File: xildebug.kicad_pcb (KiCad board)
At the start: 2 copper layers, 42 x 46.2 mm, 66 parts, among them J1 USB_B_Micro, J2 Conn_STM_SWD, J3 Conn_Ext1, J4 Conn_Ext2, J5 Conn_DUT, J6 Conn_DUT_VDD, SW1 BOOT0, U1 XC6206P332MR, U2 MAX14662, U3 STM32L433CCUx, U4 TS5A3167, U5 MIC5219YMT, U6 TS5A3167, U7 MCP4018, U8 TS5A3167

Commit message: Minification
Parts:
- removed C11, C15: 1uF, Capacitor_SMD:C_0603_1608Metric
- removed C12, C14, C17, C18, C19, C8: 0.1uF, Capacitor_SMD:C_0603_1608Metric
- removed C13: 4.7uF, Capacitor_SMD:C_0603_1608Metric
- removed C16: 470pF, Capacitor_SMD:C_0603_1608Metric
- removed D4: LED_RGB, LED_SMD_Extra:LED_RGB_0606_1616Metric
- removed the G*** at (228.9, 85.4)
- removed the G*** at (226.4, 62.4)
- removed J4: Conn_Ext2, Connector_PinHeader_2.54mm:PinHeader_1x12_P2.54mm_Vertical
- removed J6: Conn_DUT_VDD, Connector_PinHeader_2.54mm:PinHeader_1x03_P2.54mm_Horizontal
- removed L1: FB, Inductor_SMD:L_0603_1608Metric
- removed R11, R15, R17: 10K, Resistor_SMD:R_0603_1608Metric
- removed R12, R14: TBD, Resistor_SMD:R_0603_1608Metric
- removed R13: 510R, Resistor_SMD:R_0603_1608Metric
- removed R16: 33R, Resistor_SMD:R_0603_1608Metric
- removed R18: 1.8R, Resistor_SMD:R_0603_1608Metric
- removed R19, R20, R21, R22: 100K, Resistor_SMD:R_0603_1608Metric
- removed R4, R5, R6: 360R, Resistor_SMD:R_0603_1608Metric
- removed U4, U6, U8: TS5A3167, Package_TO_SOT_SMD:SOT-23-5
- removed U5: MIC5219YMT, Package_TO_SOT_SMD:SOT-23-5
- removed U7: MCP4018, Package_TO_SOT_SMD:SOT-363_SC-70-6
- added G***: LOGO, Symbol_Extra:xil_5000, B.Cu at (220.0, 86.7)
- added G***: LOGO, Symbol_Extra:oshw_crop_10000, F.Cu at (227.8, 93.0)
- added Q1: FDN340P, Package_TO_SOT_SMD:SOT-23, F.Cu at (211.1, 66.2)
- J2: footprint Connector_PinHeader_2.54mm:PinHeader_1x04_P2.54mm_Vertical -> Connector_JST:JST_SH_BM04B-SRSS-TB_1x04-1MP_P1.00mm_Vertical
- J3: value Conn_Ext1 -> Conn_GPIO; footprint Connector_PinHeader_2.54mm:PinHeader_1x11_P2.54mm_Vertical -> Connector_PinHeader_2.54mm:PinHeader_1x04_P2.54mm_Vertical
- moved J3 33.7 mm to (229.4, 74.2)
- moved D6 18.7 mm to (219.7, 68.2), turned to 270 degrees
- moved C9 18.5 mm to (211.1, 89.0)
- moved U1 18.5 mm to (211.1, 86.5), turned to 180 degrees
- moved D5 16.9 mm to (221.6, 68.2), turned to 90 degrees
- moved D1 16.6 mm to (210.2, 76.8)
- moved D2 16.6 mm to (210.2, 70.3)
- moved D3 16.6 mm to (210.2, 73.6)
- moved R1 13.3 mm to (211.8, 76.8)
- moved R2 13.3 mm to (211.8, 70.3)
- moved R3 13.3 mm to (211.8, 73.5)
- moved U2 11.2 mm to (220.0, 73.6)
- moved J2 10.4 mm to (228.6, 87.5), turned to 270 degrees
- moved R23 9.76 mm to (222.2, 78.8), turned to 90 degrees
- moved C3 7.58 mm to (217.9, 68.2), turned to 90 degrees
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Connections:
- net /POT_SCL renamed /STM_SCL
- net /POT_SDA renamed /STM_SDA
- C7 pad 1: Net-(C11-Pad1) -> +3V3
- D5 pad 1: /DUT_UART_TX_B -> Net-(D5-Pad1)
- D5 pad 2: Net-(D5-Pad2) -> /DUT_UART_RX_B
- D6 pad 1: Net-(D6-Pad1) -> /DUT_UART_TX_B
- D6 pad 2: /DUT_UART_RX_B -> Net-(D6-Pad2)
- J3 pad 1: +5V -> /GPIO0_B
- J3 pad 2: +3V3 -> /GPIO1_B
- J3 pad 3: GND -> /GPIO2_B
- J3 pad 4: /PB15 -> /GPIO3_B
- J5 pad 1: /DUT_VDD_OUT -> Net-(J5-Pad1)
- U2 pad 18: /DUT_SWCLK_B -> Net-(D5-Pad1)
- U2 pad 2: /DUT_UART_RX_A -> /DUT_SWCLK_A
- U2 pad 20: Net-(D5-Pad2) -> Net-(D6-Pad2)
- U2 pad 21: Net-(D6-Pad1) -> /DUT_SWCLK_B
- U2 pad 5: /DUT_SWCLK_A -> /DUT_UART_RX_A
- U3 pad 10: /DUT_VDD_IN_DIV -> Net-(U3-Pad10)
- U3 pad 11: /DUT_VDD_OUT_DIV -> Net-(U3-Pad11)
- U3 pad 12: /PA2 -> /DUT_UART_TX_A
- U3 pad 13: /PA3 -> /DUT_UART_RX_A
- U3 pad 14: /DUT_SWD_LED -> /DUT_SWDIO_A
- U3 pad 15: /SHUNT1_EN -> /DUT_SWCLK_A
- U3 pad 16: /SHUNT2_EN -> /DUT_VDD_CTRL
- U3 pad 17: /PA7 -> /DUT_UART_TX_LED
- U3 pad 18: /DUT_VDD_EN -> /DUT_UART_RX_LED
- U3 pad 19: /DUT_SWCLK_A -> /DUT_SWD_LED
- U3 pad 2: /GPIO2_A -> Net-(U3-Pad2)
- U3 pad 20: /DUT_SWDIO_A -> Net-(U3-Pad20)
- U3 pad 21: /DUT_UART_TX_A -> Net-(U3-Pad21)
- U3 pad 22: /DUT_UART_RX_A -> Net-(U3-Pad22)
- U3 pad 25: /LED_RGB_B -> Net-(U3-Pad25)
- U3 pad 26: /PB13 -> Net-(U3-Pad26)
- U3 pad 27: /PB14 -> Net-(U3-Pad27)
- U3 pad 28: /PB15 -> Net-(U3-Pad28)
- U3 pad 29: /LED_RGB_G -> Net-(U3-Pad29)
- U3 pad 3: /GPIO3_A -> /GPIO0_A
- U3 pad 38: /LED_RGB_R -> Net-(U3-Pad38)
- U3 pad 39: /PB3 -> Net-(U3-Pad39)
- U3 pad 4: /PC15 -> /GPIO1_A
- U3 pad 40: /PB4 -> Net-(U3-Pad40)
- U3 pad 41: /PB5 -> Net-(U3-Pad41)
- U3 pad 42: /PB6 -> Net-(U3-Pad42)
- U3 pad 43: /PB7 -> Net-(U3-Pad43)
- U3 pad 45: /GPIO0_A -> Net-(U3-Pad45)
- U3 pad 46: /GPIO1_A -> Net-(U3-Pad46)
- U3 pad 5: /DUT_UART_TX_LED -> /GPIO2_A
- U3 pad 6: /DUT_UART_RX_LED -> /GPIO3_A
- U3 pad 9: Net-(C11-Pad1) -> +3V3
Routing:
- net +5V: track 88.7 -> 15.8 mm, vias 7 -> 2
- net +3V3: track 176.9 -> 112.3 mm, vias 15 -> 17
- net /DUT_VDD_OUT: track 48.1 -> 0.00 mm, vias 1 -> 0
- net /DUT_VDD_IN: track 43.6 -> 0.00 mm, vias 2 -> 0
- net /SHUNT1_EN: track 40.4 -> 0.00 mm, vias 3 -> 0
- net /LED_RGB_R: track 39.0 -> 0.00 mm, vias 4 -> 0
- net /DUT_VDD_EN: track 37.5 -> 0.00 mm, vias 2 -> 0
- net /PC15: track 36.4 -> 0.00 mm, vias 1 -> 0
- net /SHUNT2_EN: track 34.5 -> 0.00 mm, vias 2 -> 0
- net /PB13: track 29.5 -> 0.00 mm
- net /PB14: track 28.0 -> 0.00 mm
- net /PB15: track 26.5 -> 0.00 mm
- net /LED_RGB_G: track 24.9 -> 0.00 mm, vias 2 -> 0
- net /PA2: track 22.9 -> 0.00 mm, vias 1 -> 0
- net /LED_RGB_B: track 22.2 -> 0.00 mm, vias 2 -> 0
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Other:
- board size 42 x 46.2 mm -> 22.4 x 39.7 mm
- board text added: "0"
- board text added: "1"
- board text added: "2"
- board text added: "3"
- board text added: "@arturo182"
- board text added: "BOOT0"
- board text added: "GPIO"
- board text added: "VDD"
- board text added: "xildebug mini rev1"
- board text removed: "3.3V"
- board text removed: "3V"
- board text removed: "5V"
- board text removed: "A2"
- board text removed: "A3"
- board text removed: "A7"
- board text removed: "B13"
- board text removed: "B14"
- board text removed: "B15"
- board text removed: "B3"
- board text removed: "B4"
- board text removed: "B5"
- board text removed: "B6"
- board text removed: "B7"
- board text removed: "C15"
- board text removed: "GPIO0/B8"
- board text removed: "GPIO1/B9"
- board text removed: "GPIO2/C13"
- board text removed: "GPIO3/C14"
- board text removed: "Vdut"
- board text removed: "Vin"
- board text removed: "Vreg"
- board text removed: "xildebug rev1 Apr 2018"

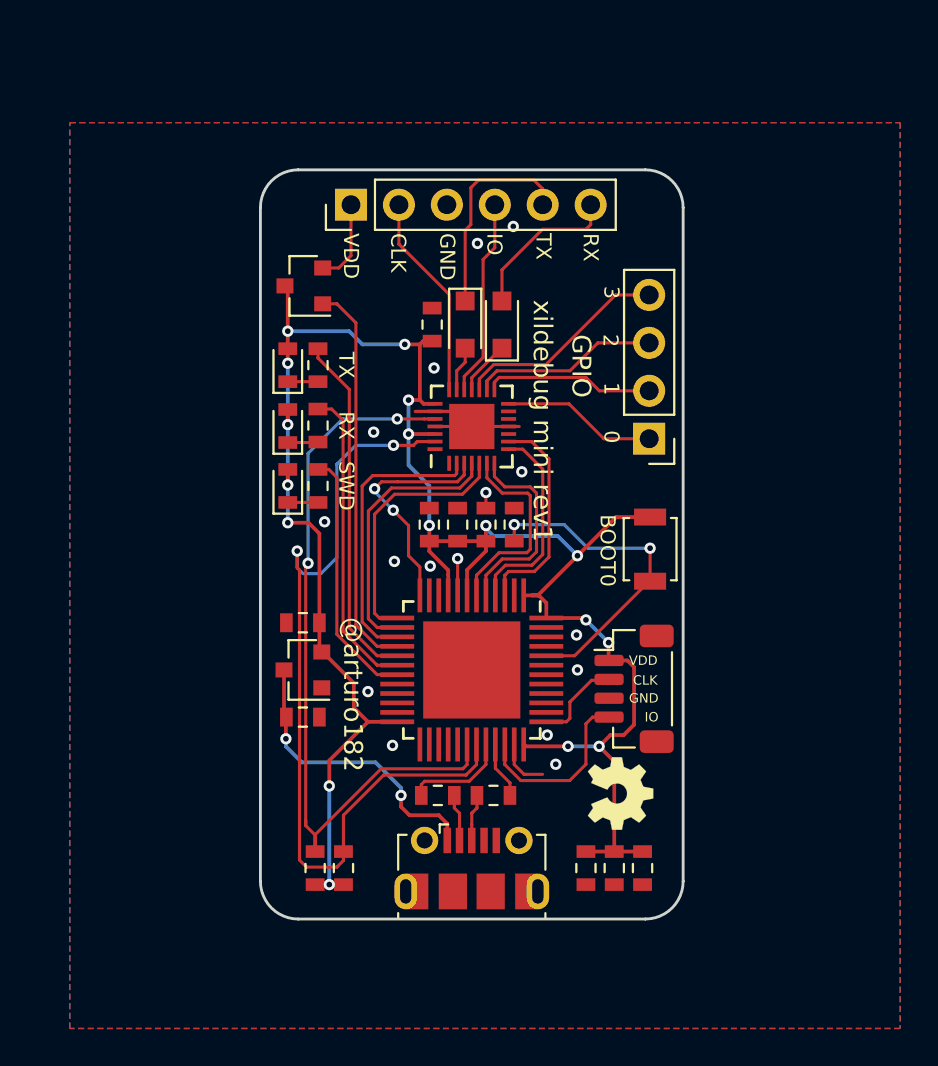
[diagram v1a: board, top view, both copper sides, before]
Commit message: rev2
- Replaced the VDD mosfet with a analog switch
- Changed footprint of STM32L433 to standard one
- Moved UART to USART3, same as xildebug big
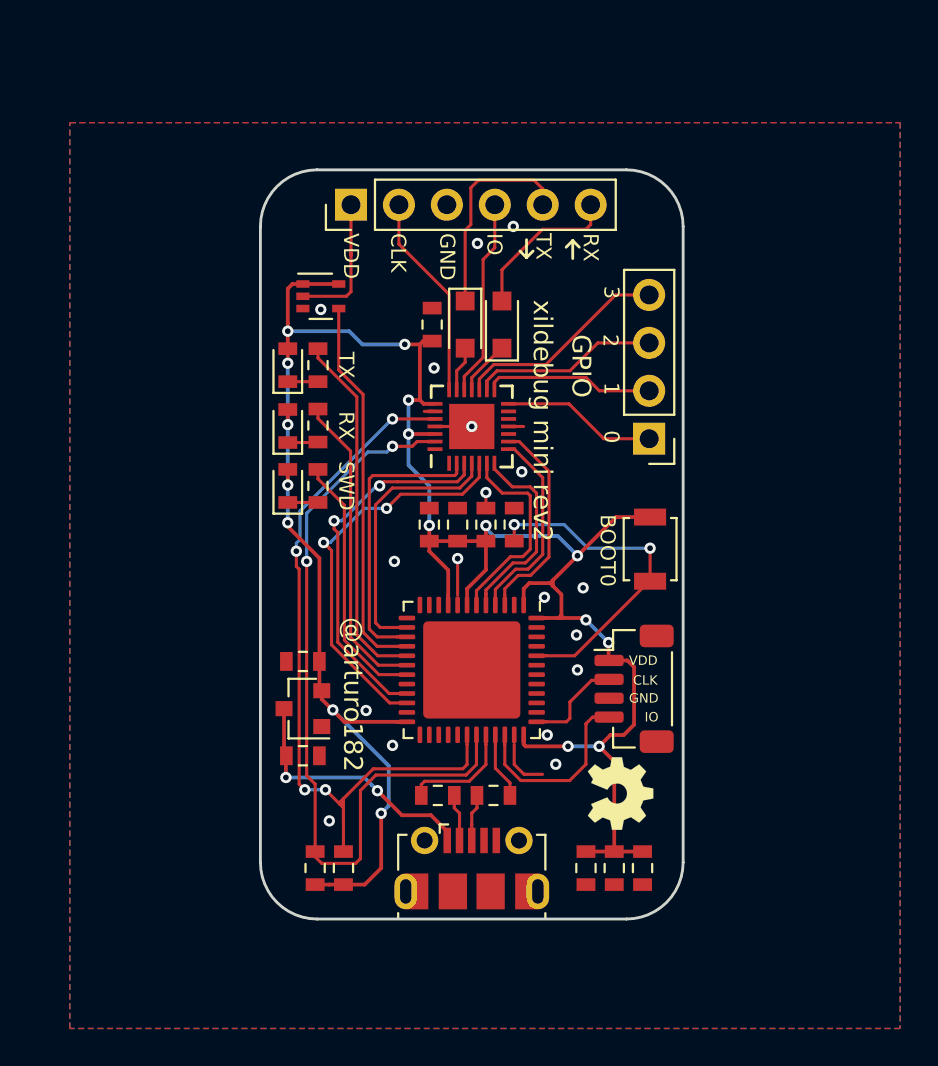
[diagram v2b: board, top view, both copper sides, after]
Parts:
- removed Q1: FDN340P, Package_TO_SOT_SMD:SOT-23
- added U4: SN74LVC1G66, Package_TO_SOT_SMD_Extra:SC-70-5, F.Cu at (212.0, 66.7)
- U3: footprint Package_DFN_QFN_Extra:UFQFPN-48-1EP_7x7mm_P0.5mm_EP5.15x5.15mm -> Package_DFN_QFN:QFN-48-1EP_7x7mm_P0.5mm_EP5.15x5.15mm
- moved C1 2.05 mm to (211.1, 86.0)
- moved C9 2.05 mm to (211.1, 91.0)
- moved U1 2.05 mm to (211.1, 88.5)
- moved R10 1.50 mm to (213.2, 97.0)
- moved R9 1.50 mm to (211.7, 97.0)
- turned G*** to 90 degrees
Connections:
- U3 pad 12: /DUT_UART_TX_A -> Net-(U3-Pad12)
- U3 pad 13: /DUT_UART_RX_A -> Net-(U3-Pad13)
- U3 pad 21: Net-(U3-Pad21) -> /DUT_UART_TX_A
- U3 pad 22: Net-(U3-Pad22) -> /DUT_UART_RX_A
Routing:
- net +3V3: track 112.3 -> 121.8 mm
- net /DUT_UART_RX_A: track 13.7 -> 21.3 mm, vias 0 -> 2
- net /DUT_UART_TX_A: track 12.3 -> 19.8 mm
- net /STM_SDA: track 44.8 -> 41.3 mm
- net GND: track 13.4 -> 10.0 mm, vias 16 -> 18
- net Net-(J5-Pad1): track 4.47 -> 7.41 mm
- net +5V: track 15.8 -> 13.9 mm
- net /STM_SCL: track 40.6 -> 39.7 mm, vias 2 -> 4
- net /DUT_VDD_CTRL: track 20.8 -> 20.3 mm
- net Net-(R8-Pad2): track 5.50 -> 6.02 mm
- net Net-(R7-Pad2): track 3.02 -> 3.53 mm
- net /STM_SWDIO: track 9.59 -> 10.1 mm
- net Net-(R23-Pad1): track 17.5 -> 18.0 mm
- net /STM_SWCLK: track 4.76 -> 5.28 mm
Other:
- outline, holes or cut-outs redrawn
- board text added: "xildebug mini rev2"
- board text removed: "xildebug mini rev1"
